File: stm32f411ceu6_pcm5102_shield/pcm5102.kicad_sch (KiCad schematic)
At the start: 47 parts, among them J1 AudioJack3_Ground_SwitchTR, J2 AudioJack3_Ground_SwitchTR, Q1 BC337, Q2 BC337, U1 SW_DPDT_XLX, U2 SW_DPDT_XLX, U3 SW_DPDT_XLX, U4 SW_DPDT_XLX, U5 SW_DPDT_XLX, U6 PCM5102A, U7 HT7533-1

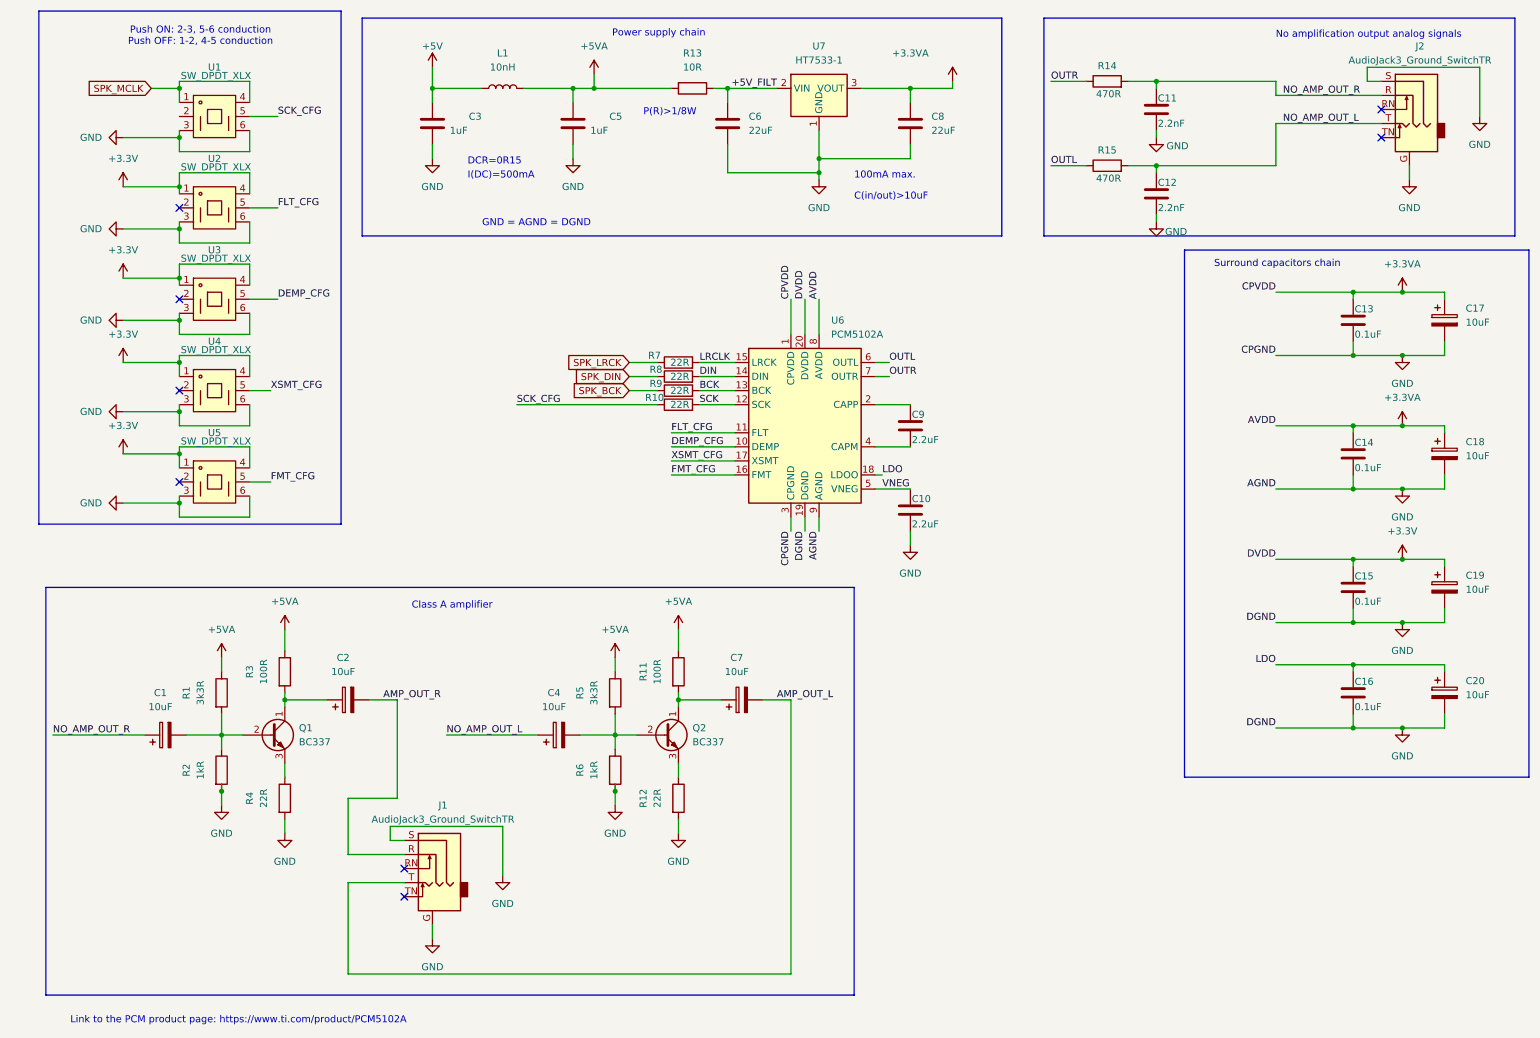
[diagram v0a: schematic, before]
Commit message: Headphone jack detection
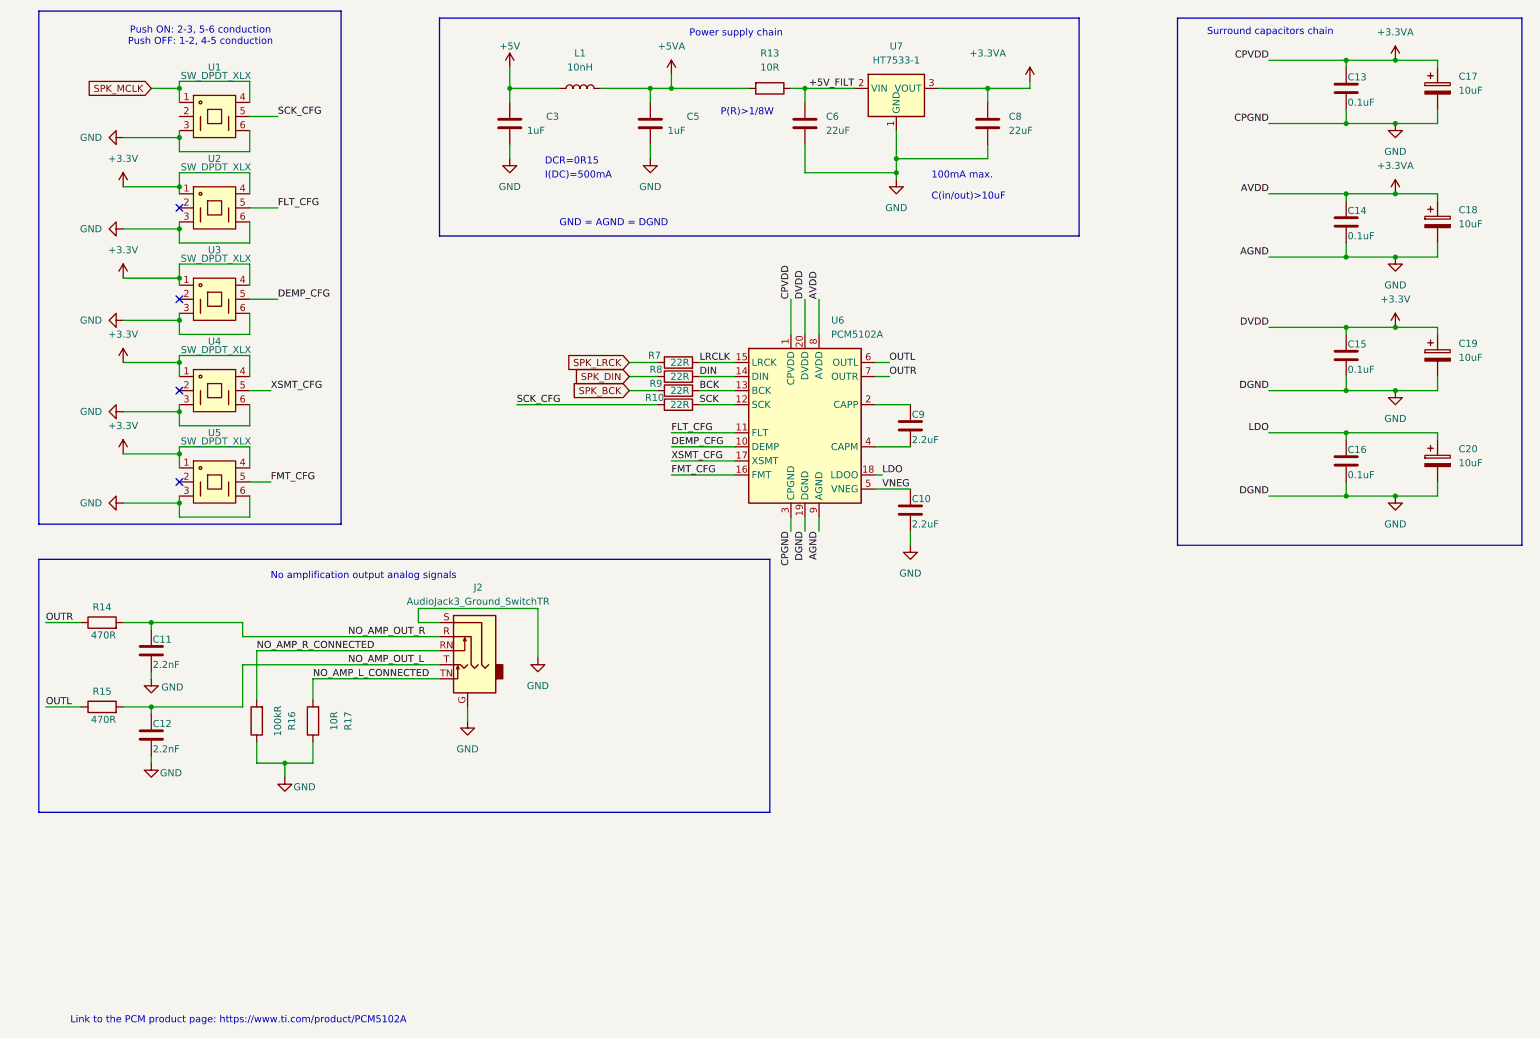
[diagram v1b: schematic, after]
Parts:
- removed C1, C2, C4, C7: 10uF, symbol Device:C_Polarized
- removed J1: AudioJack3_Ground_SwitchTR, Connector_Audio:Jack_3.5mm_PJ311_Horizontal, symbol Connector_Audio:AudioJack3_Ground_SwitchTR
- removed Q1, Q2: BC337, Package_TO_SOT_THT:TO-92_Inline, symbol Transistor_BJT:BC337
- removed R1, R5: 3k3R, Resistor_SMD:R_0805_2012Metric, symbol Device:R
- removed R11, R3: 100R, Resistor_SMD:R_0805_2012Metric, symbol Device:R
- removed R12, R4: 22R, Resistor_SMD:R_0805_2012Metric, symbol Device:R
- removed R2, R6: 1kR, Resistor_SMD:R_0805_2012Metric, symbol Device:R
- added R16: 100kR, Resistor_SMD:R_0805_2012Metric, symbol Device:R
- added R17: 10R, Resistor_SMD:R_0805_2012Metric, symbol Device:R
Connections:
- net GND: now also R16.1, R17.1
- net NO_AMP_R_CONNECTED: now reaches J2.RN
- net NO_AMP_R_CONNECTED: now also R16.2
- net NO_AMP_L_CONNECTED: now reaches J2.TN
- net NO_AMP_L_CONNECTED: now also R17.2
- no-connect marks 8 -> 4
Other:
- note removed: "Class A amplifier"
- moved on the sheet: C11, C12, C13, C14, C15, C16, C17, C18, C19, C20, C3, C5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

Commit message: Add rotary encoder
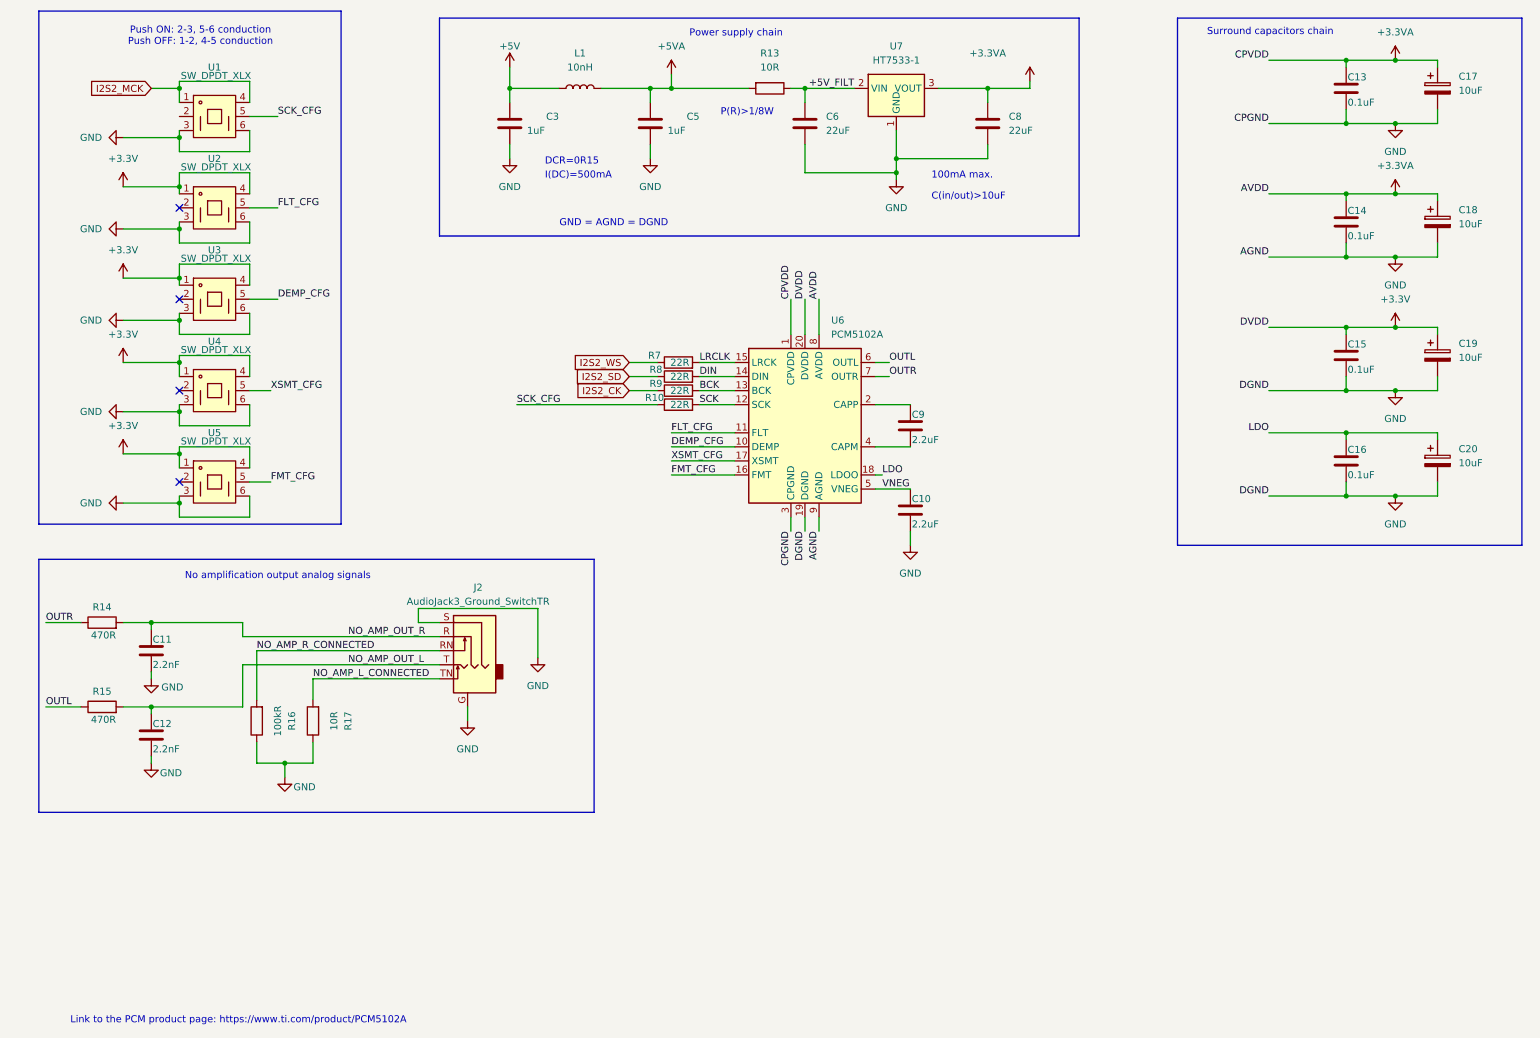
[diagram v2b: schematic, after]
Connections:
- net SPK_BCK renamed I2S2_CK
- net SPK_DIN renamed I2S2_SD
- net SPK_LRCK renamed I2S2_WS
- net SPK_MCLK renamed I2S2_MCK
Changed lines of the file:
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@@
 	(rectangle
 		(start 13.97 111.76)
-		(end 146.05 157.48)
+		(end 114.3 157.48)
 		(stroke
 			(width 0)
@@
 	(text "No amplification output analog signals"
 		(exclude_from_sim no)
-		(at 72.644 114.808 0)
+		(at 57.15 114.808 0)
 		(effects
 			(font
@@
 		)
 	)
-	(global_label "SPK_BCK"
+	(global_label "I2S2_CK"
 		(shape input)
 		(at 120.65 81.28 180)
@@
 		)
 		(property "Intersheetrefs" "${INTERSHEET_REFS}"
-			(at 109.1377 81.28 0)
+			(at 109.9239 81.28 0)
 			(effects
 				(font
@@
 		)
 	)
-	(global_label "SPK_MCLK"
+	(global_label "I2S2_SD"
 		(shape input)
-		(at 34.29 26.67 180)
+		(at 120.65 78.74 180)
 		(fields_autoplaced yes)
 		(effects
@@
 		)
 		(property "Intersheetrefs" "${INTERSHEET_REFS}"
-			(at 21.5682 26.67 0)
+			(at 109.9844 78.74 0)
 			(effects
 				(font
@@
 		)
 	)
-	(global_label "SPK_LRCK"
+	(global_label "I2S2_WS"
 		(shape input)
 		(at 120.65 76.2 180)
@@
 		)
 		(property "Intersheetrefs" "${INTERSHEET_REFS}"
-			(at 108.1096 76.2 0)
+			(at 109.803 76.2 0)
 			(effects
 				(font
@@
 		)
 	)
-	(global_label "SPK_DIN"
+	(global_label "I2S2_MCK"
 		(shape input)
-		(at 120.65 78.74 180)
+		(at 34.29 26.67 180)
 		(fields_autoplaced yes)
 		(effects
@@
 		)
 		(property "Intersheetrefs" "${INTERSHEET_REFS}"
-			(at 109.7424 78.74 0)
+			(at 22.1125 26.67 0)
 			(effects
 				(font

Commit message: Items numeration fix
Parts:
- renumbered C3 to C200, C5 to C201, C6 to C202, C8 to C203, C13 to C204, C17 to C205, C14 to C206, C18 to C207, C15 to C208, C19 to C209, C16 to C210, C20 to C211, C11 to C213, C12 to C214, C9 to C215, C10 to C216, J2 to J200, L1 to L200, R13 to R200, R14 to R201, R15 to R202, R16 to R203, R17 to R204, U1 to SW200, U2 to SW201, U3 to SW202, U4 to SW203, U5 to SW204, U6 to U200, U7 to U201

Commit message: BOM updates
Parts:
- removed R203: 100kR, Resistor_SMD:R_0805_2012Metric, symbol Device:R
- removed R204: 10R, Resistor_SMD:R_0805_2012Metric, symbol Device:R
- C200, C201: footprint Capacitor_SMD:C_0603_1608Metric -> Capacitor_SMD:C_0805_2012Metric; Manufacturer Samwha Capacitor -> Samsung Electro-Mechanics; Manufacturer Part Number CS1608Y5V105Z160NRB -> CL21B105KBFNNNE
- C202, C203: Manufacturer Samwha Capacitor -> Samsung Electro-Mechanics; Manufacturer Part Number CS2012X5R226M160NRE -> CL21A226MQQNNNE
- C204, C206, C208, C210: value 0.1uF -> 100nF; footprint (none) -> Capacitor_SMD:C_0805_2012Metric; Manufacturer (none) -> Samsung Electro-Mechanics; Manufacturer Part Number (none) -> CL21B104KBCNNNC
- C205, C207, C209, C211: footprint (none) -> Capacitor_Tantalum_SMD:CP_EIA-3216-18_Kemet-A; Manufacturer (none) -> Kyocera AVX; Manufacturer Part Number (none) -> TAJA106K016RNJ
- C213, C214: footprint (none) -> Capacitor_SMD:C_0805_2012Metric; Manufacturer (none) -> Samsung Electro-Mechanics; Manufacturer Part Number (none) -> CL21C222JBFNNNE
- C215, C216: footprint (none) -> Capacitor_SMD:C_0805_2012Metric; Manufacturer (none) -> Samsung Electro-Mechanics; Manufacturer Part Number (none) -> CL21B225KAFNNNE
- R10, R7, R8, R9: footprint (none) -> Resistor_SMD:R_0805_2012Metric; Manufacturer (none) -> UNI-ROYAL(Uniroyal Elec); Manufacturer Part Number (none) -> 0805W8F220JT5E
- R201, R202: footprint (none) -> Resistor_SMD:R_0805_2012Metric; Manufacturer (none) -> UNI-ROYAL(Uniroyal Elec); Manufacturer Part Number (none) -> 0805W8F4700T5E
- SW200, SW201, SW202, SW203, SW204: Manufacturer (none) -> SHOU HAN; Manufacturer Part Number (none) -> 8-8 ZS
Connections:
- no-connect marks 4 -> 5

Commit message: Put all items on a board
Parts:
- J200: footprint Connector_Audio:Jack_3.5mm_PJ311_Horizontal -> stm32f401_pcm5102_shiled_lib:AudioJack_3.5mm_PJ311
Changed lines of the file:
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@@
 			)
 		)
-		(property "Footprint" "Connector_Audio:Jack_3.5mm_PJ311_Horizontal"
+		(property "Footprint" "stm32f401_pcm5102_shiled_lib:AudioJack_3.5mm_PJ311"
 			(at 91.44 125.73 0)
 			(effects

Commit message: PCB rules setup
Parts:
- added J201: Conn_01x03_Pin, Connector_PinHeader_2.54mm:PinHeader_1x03_P2.54mm_Vertical, symbol Connector:Conn_01x03_Pin
- C204, C206, C208, C210: footprint Capacitor_SMD:C_0805_2012Metric -> Capacitor_SMD:C_0402_1005Metric; Manufacturer Part Number CL21B104KBCNNNC -> CL05B104KO5NNNC
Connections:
- net GND: now also J201.1 (Pin_1)
- net NO_AMP_OUT_L: now also J201.2 (Pin_2)
- net NO_AMP_OUT_R: now also J201.3 (Pin_3)

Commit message: Initial layout
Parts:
- removed C204, C206, C208: 100nF, Capacitor_SMD:C_0402_1005Metric, symbol Device:C
- removed C205, C207, C209: 10uF, Capacitor_Tantalum_SMD:CP_EIA-3216-18_Kemet-A, symbol Device:C_Polarized
- added C1, C2, C3: 100nF, Capacitor_SMD:C_0402_1005Metric, symbol Device:C
- added C4, C5, C6: 10uF, Capacitor_Tantalum_SMD:CP_EIA-3216-18_Kemet-A, symbol Device:C_Polarized
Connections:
- net +3.3V: now also U200.8 (AVDD), C3.1, C6.1; no longer U200.20 (DVDD)
- net +3.3VA: now also U200.20 (DVDD), C1.1, C2.1, C4.1, C5.1; no longer U200.8 (AVDD)
- net GND: now also C1.2, C2.2, C3.2, C4.2, C5.2, C6.2
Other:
- note removed: "Surround capacitors chain"
- moved on the sheet: C210, C211

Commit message: Initial layout
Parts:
- removed SW201, SW202, SW203, SW204: SW_DPDT_XLX, stm32f401_pcm5102_shiled_lib:SW_DPDT_XLX, symbol stm32f401_pcm5102_shiled_lib:SW_DPDT_XLX
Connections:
- net DEMP_CFG is gone; now on net GND: U200.10 (DEMP)
- net FLT_CFG is gone; now on net GND: U200.11 (FLT)
- net FMT_CFG is gone; now on net GND: U200.16 (FMT)
- net XSMT_CFG is gone; now on net +3.3V: U200.17 (XSMT)
- no-connect marks 5 -> 1
